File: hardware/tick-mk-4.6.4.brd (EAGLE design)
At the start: 96 x 53 mm, 40 parts, among them IC1 ATMEGA328P, IC2 DS3231, IC3 L7805, Y1 16MHz

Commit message: headers swapped, layout de-fucked a bit more
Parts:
- removed U$3: (no value), A_butts:COW_SMALL
- added C9: 0.1uF, A_butts:C025-024X044
- JP1: value FTDI_CONNJST_PH_VERT_PTH_LESSSILK -> FTDI_CONNFLIPPER; device A_butts:FTDI_CONN_JST_PH_RA_PTH_LESSSILK -> A_butts:FTDI_CONN_FLIP
- moved AVR_ISP 1.00 mm to (64.0, 41.0)
- moved C3 1.00 mm to (70.5, 41.0)
- moved R1 0.50 mm to (34.5, 31.0)
- moved JP1 0.20 mm to (1.80, 14.0)
- renumbered S1 to RESET
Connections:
- new net N$1: C9.2, IC1.21
- net GND: now also C9.1
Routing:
- net D9: track 143.2 -> 148.0 mm, vias 6 -> 5
- net N$1: track 0.00 -> 3.35 mm
- net A0: track 161.2 -> 164.0 mm, vias 5 -> 4
- net A1: track 149.7 -> 152.4 mm
- net VCC: track 150.5 -> 147.8 mm
- net D10: track 119.8 -> 122.3 mm, vias 3 -> 4
- net RST: track 93.3 -> 92.1 mm
- net D13/SCK: track 182.3 -> 183.3 mm
- net D11/MOSI: track 162.9 -> 163.5 mm
- net D12/MISO: track 212.9 -> 213.5 mm

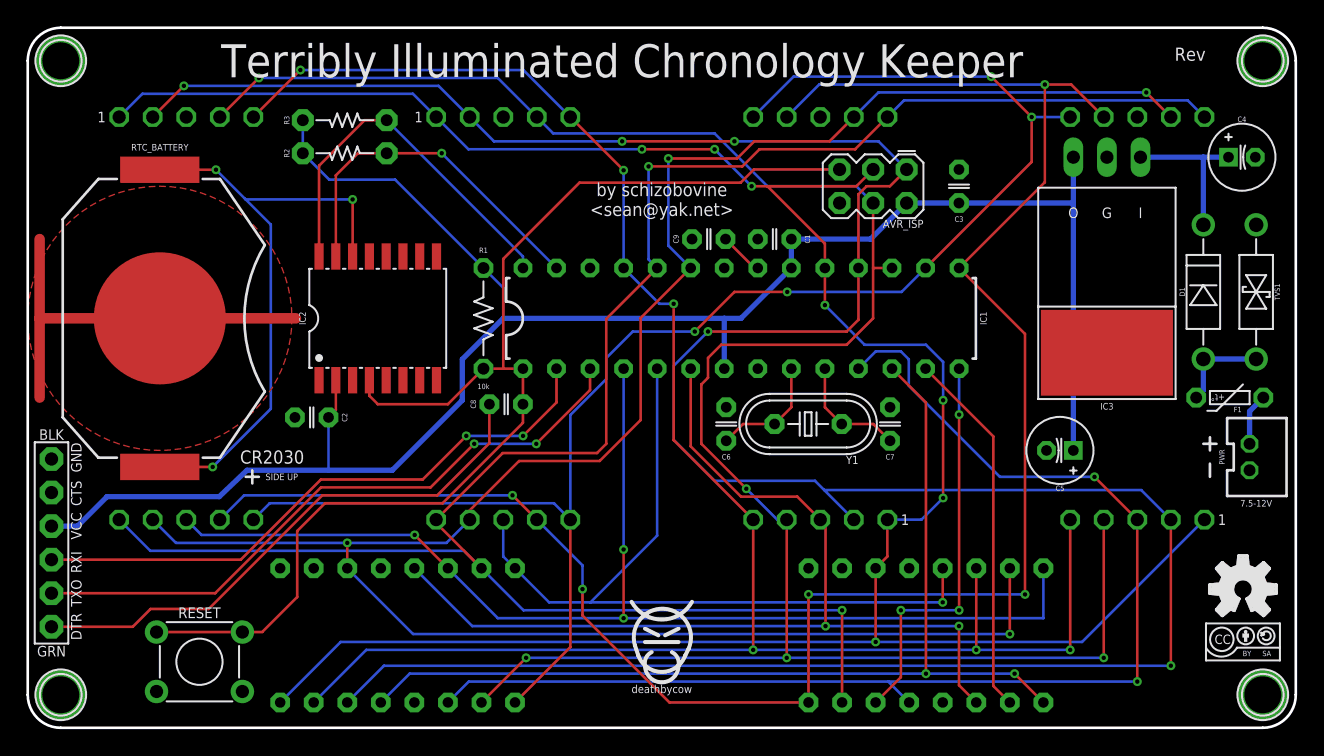
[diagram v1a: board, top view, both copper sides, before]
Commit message: tweaks to silkscreen and traces
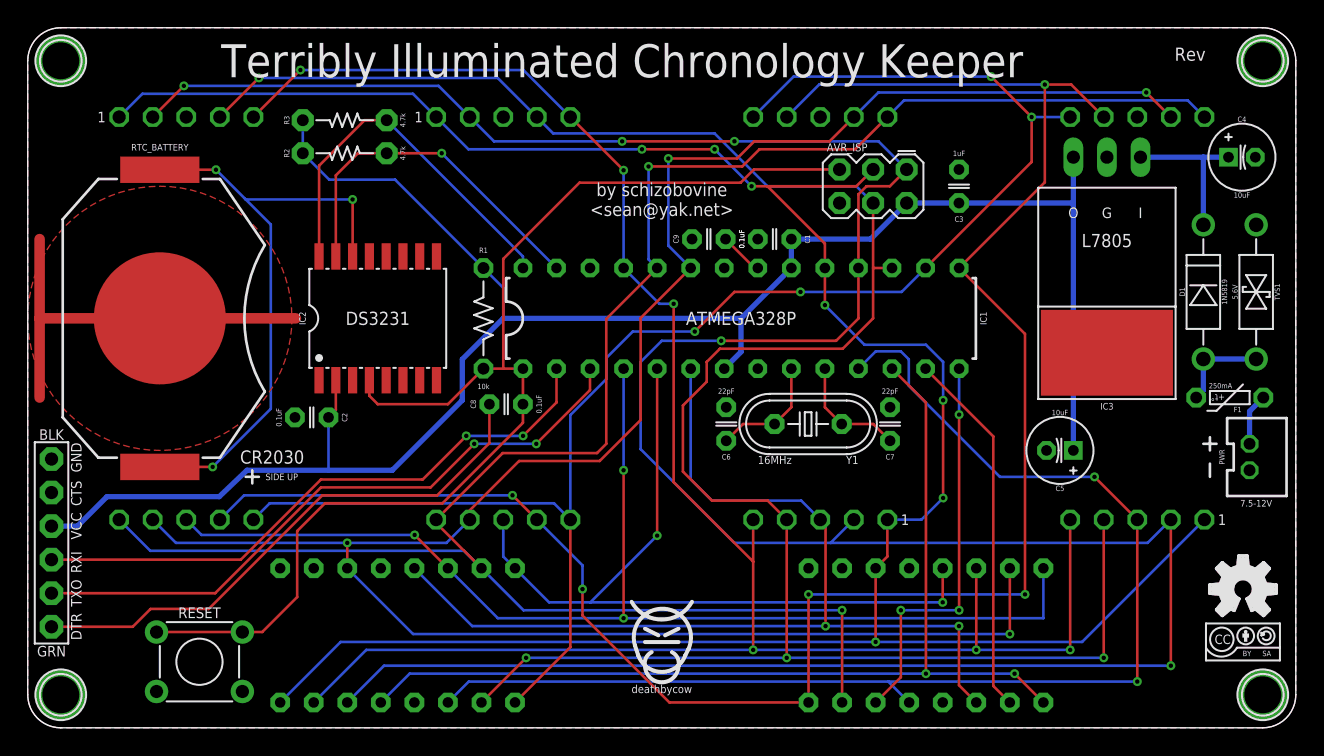
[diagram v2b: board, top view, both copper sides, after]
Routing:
- net D12/MISO: track 213.5 -> 219.8 mm
- net A2: track 148.6 -> 151.8 mm
- net D11/MOSI: track 163.5 -> 166.6 mm, vias 5 -> 4
- net D4: track 75.6 -> 77.0 mm
- net VCC: track 147.8 -> 148.4 mm
- net D3: vias 1 -> 2
